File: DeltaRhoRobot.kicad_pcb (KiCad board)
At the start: 4 copper layers, 75 x 100 mm, 135 parts, among them J1 Conn_01x02_Socket, J10 Conn_01x02, J11 Conn_01x08, J12 USB_C_Receptacle_USB2.0, J13 Conn_02x09_Top_Bottom, J14 Conn_01x09, J15 Conn_02x09_Top_Bottom, J2 USB_C_Receptacle_USB2.0, J3 USB_C_Receptacle_USB2.0, J4 JST-XH, J5 JST-XH, J6 Conn_01x09, J7 Conn_02x20_Counter_Clockwise, P1 B6B-ZRLFSN, P2 B6B-ZRLFSN, P3 B6B-ZRLFSN, P4 B6B-ZRLFSN, P5 B6B-ZRLFSN, P6 B6B-ZRLFSN, Q2 BSS138, Q5 BSS138, SW1 CAS-120A1, SW4 SW_Push, U10 ICM-42688-P, U11 LIS3MDL, U12 ESP32-CAM, U13 MIC5365-3.3YC5, U14 W25Q16JVS, U2 AMS1117-3.3, U3 DRV8835DSSR, U4 RP2040, U5 DRV8835DSSR, U6 DRV8835DSSR, U7 TPS566242DRLR, U8 ESP32-S3-WROOM-1-N8R2, U9 FT231XQ, Y1 ABM8-272-T3

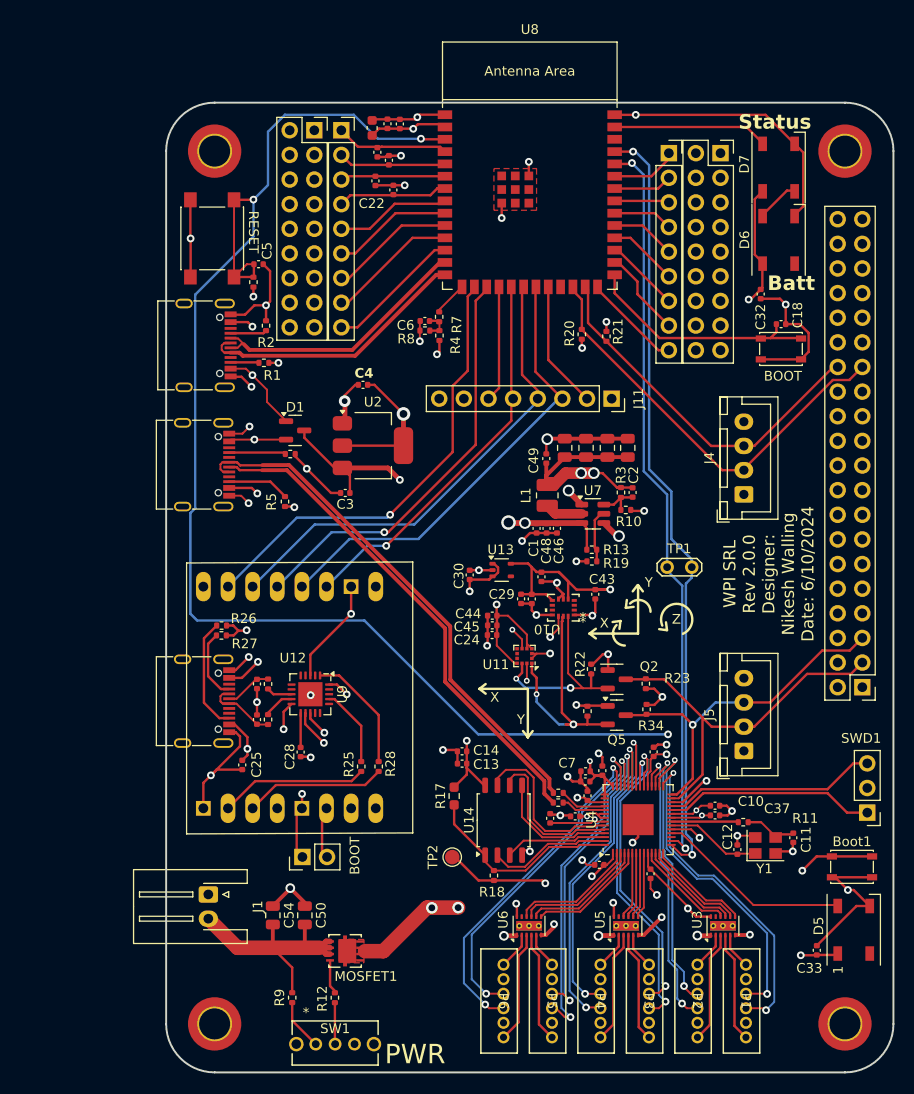
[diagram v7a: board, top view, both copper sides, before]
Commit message: Fixing issues
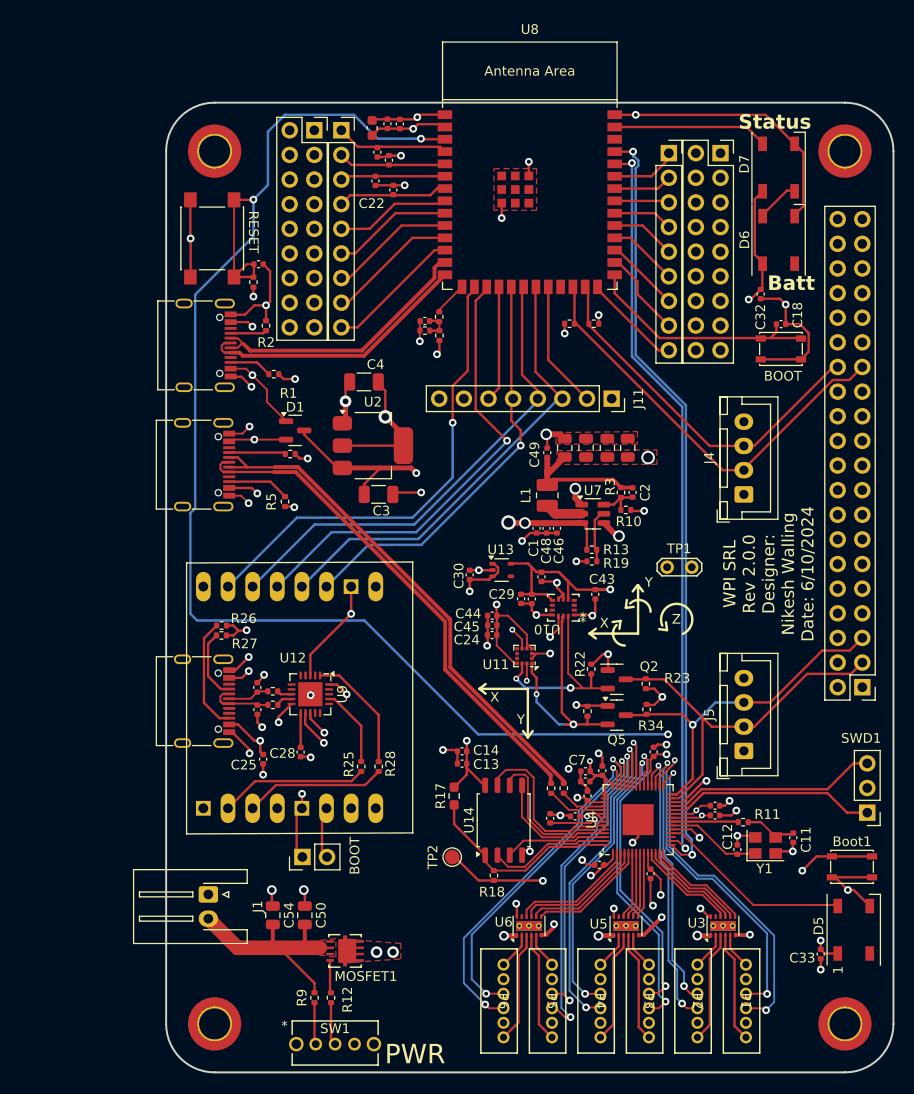
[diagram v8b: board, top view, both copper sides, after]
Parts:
- C3, C4: footprint Capacitor_SMD:C_0402_1005Metric -> Capacitor_SMD:C_1206_3216Metric
- R15: value 33 -> 27
- moved C3 3.43 mm to (171.9, 90.4), turned to 0 degrees
- moved R9 2.30 mm to (165.3, 142.3)
- moved C25 2.23 mm to (160.0, 117.7)
- moved R21 1.84 mm to (194.1, 72.8), turned to 180 degrees
- moved R20 1.67 mm to (191.6, 72.8), turned to 0 degrees
- moved R15 1.64 mm to (189.7, 120.7), turned to -90 degrees
- moved R29 1.60 mm to (161.0, 112.1), turned to 0 degrees
- moved R1 1.55 mm to (161.1, 78.0)
- moved C27 1.02 mm to (159.4, 112.6), turned to -90 degrees
- moved R30 0.90 mm to (161.0, 110.7), turned to 180 degrees
- moved R16 0.74 mm to (191.0, 120.7), turned to -90 degrees
- moved C49 0.61 mm to (189.3, 86.1)
- moved C33 0.56 mm to (217.5, 137.8), turned to 90 degrees
- moved R12 0.40 mm to (167.0, 142.3)
- moved C26 0.35 mm to (159.4, 110.3), turned to 90 degrees
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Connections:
- R15 pad 1: /Pico/USB_DM_Pico -> /Pico/USB_DP_Pico
- R16 pad 1: Net-(U4-USB_DM) -> /Pico/USB_DM_Pico
- R16 pad 2: /Pico/USB_DP_Pico -> Net-(U4-USB_DM)
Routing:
- net Earth: track 242.9 -> 216.4 mm, vias 57 -> 63
- net +5V: track 199.7 -> 174.2 mm, vias 5 -> 4
- net +3.3V: track 92.9 -> 86.5 mm, vias 17 -> 18
- net VCC: track 132.9 -> 127.5 mm
- net /ESP32-S3-WROOM-1/ESP_CS1: track 43.0 -> 47.3 mm
- net /ESP32-S3-WROOM-1/ESP32CAM/V_USB: track 29.3 -> 25.7 mm
- net /ESP32-S3-WROOM-1/ESP_MOSI: track 39.9 -> 42.8 mm
- net /Pico/USB_DP_Pico: track 54.9 -> 52.3 mm
- net VIN: track 26.6 -> 24.3 mm
- net Net-(U4-USB_DP): track 4.60 -> 6.24 mm
- net Net-(U9-USBDM): track 3.19 -> 1.61 mm
- net Net-(J2-CC2): track 2.92 -> 4.49 mm
- net /ESP32-S3-WROOM-1/Handshake: track 46.3 -> 47.8 mm
- net Net-(SW1-A): track 5.44 -> 4.15 mm
- net Net-(U9-USBDP): track 2.65 -> 1.55 mm
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- added copper zone on F.Cu, net +5V
- added copper zone on In2.Cu, net +5V
- added copper zone on F.Cu, net VIN
